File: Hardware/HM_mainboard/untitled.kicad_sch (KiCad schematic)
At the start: 13 parts, among them J1 JST PH2P ST90, Q1 PMOS - AS3401, U1 MCP73831-2, U2 TC1262-33

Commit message: Added BOM
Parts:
- C5: value 1.0UF-25V-(+80/-20%) -> 1.0uF-25V-(+80/-20%)
- C5: value 4.7u -> 4.7uF
- D2: Mouser (none) -> 10BQ015; Mouser Price/Stock (none) -> https://eu.mouser.com/ProductDetail/Vishay-Semiconductors/V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
- J1: Mouser Price/Stock (none) -> https://www.reichelt.at/at/de/jst-stiftleiste-90-1x2-polig-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; Reichelt (none) -> JST PH2P ST90
- Q1: Digikey (none) -> AS3401; Mouser Price/Stock (none) -> https://www.digikey.at/de/products/detail/anbon-semiconduct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
- R6: Mouser (none) -> RN73H1JTTD1002F100; Mouser Price/Stock (none) -> https://www.mouser.at/ProductDetail/KOA-Speer/RN73H1JTTD100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
- U1: Mouser (none) -> MCP73831T-2ACI/OT; Mouser Price/Stock (none) -> https://www.mouser.at/ProductDetail/Microchip-Technology/MC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
- U2: Mouser Price/Stock (none) -> https://www.mouser.at/ProductDetail/Microchip-Technology/TC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
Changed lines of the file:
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@@
       (effects (font (size 1.27 1.27)) (justify left))
     )
-    (property "Value" "1.0UF-25V-(+80/-20%)" (at 100.965 84.455 90)
+    (property "Value" "1.0uF-25V-(+80/-20%)" (at 100.965 84.455 90)
       (effects (font (size 1.27 1.27)) (justify left))
     )
@@
       (effects (font (size 1.27 1.27)) hide)
     )
+    (property "Reichelt" "" (at 104.775 65.405 0)
+      (effects (font (size 1.27 1.27)) hide)
+    )
     (pin "1")
     (pin "2")
@@
       (effects (font (size 1.27 1.27)) (justify left))
     )
-    (property "Value" "1.0UF-25V-(+80/-20%)" (at 144.145 78.105 90)
+    (property "Value" "1.0uF-25V-(+80/-20%)" (at 144.145 78.105 90)
       (effects (font (size 1.27 1.27)) (justify left))
     )
@@
     )
     (property "Mouser" "F921E105KPA" (at 137.795 65.405 0)
+      (effects (font (size 1.27 1.27)) hide)
+    )
+    (property "Reichelt" "" (at 137.795 65.405 0)
       (effects (font (size 1.27 1.27)) hide)
     )
@@
     )
     (property "Mouser" "ERJ-PA3J121V" (at 82.55 158.75 0)
+      (effects (font (size 1.27 1.27)) hide)
+    )
+    (property "Reichelt" "" (at 82.55 158.75 0)
       (effects (font (size 1.27 1.27)) hide)
     )
@@
       (effects (font (size 1.27 1.27)) hide)
     )
+    (property "Reichelt" "" (at 200.66 130.81 0)
+      (effects (font (size 1.27 1.27)) hide)
+    )
     (pin "1")
     (pin "2")
@@
       (effects (font (size 1.27 1.27)) hide)
     )
+    (property "Mouser Price/Stock" "https://www.reichelt.at/at/de/jst-stiftleiste-90-1x2-polig-ph-jst-ph2p-st90-p185056.html?PROVID=2807&gclid=CjwKCAiAmZGrBhAnEiwAo9qHiX8Aljedun1deSYFSHEVMIRz6JgVll-Dw5EvRr3jTF0y2CSldQKAmBoCrskQAvD_BwE" (at 52.07 146.05 0)
+      (effects (font (size 1.27 1.27)) hide)
+    )
+    (property "Reichelt" "JST PH2P ST90" (at 52.07 146.05 0)
+      (effects (font (size 1.27 1.27)) hide)
+    )
     (pin "1")
     (pin "2")
@@
       (effects (font (size 1.27 1.27)) hide)
     )
+    (property "Mouser Price/Stock" "https://www.mouser.at/ProductDetail/Microchip-Technology/TC1262-3.3VDBTR?qs=VDoAoI%2FEFTN6q7dfuakIrw%3D%3D" (at 120.015 59.055 0)
+      (effects (font (size 1.27 1.27)) hide)
+    )
+    (property "Reichelt" "" (at 120.015 59.055 0)
+      (effects (font (size 1.27 1.27)) hide)
+    )
     (pin "1")
     (pin "2")
@@
       (effects (font (size 1.27 1.27)) (justify left))
     )
-    (property "Value" "4.7u" (at 68.58 149.86 0)
+    (property "Value" "4.7uF" (at 68.58 149.86 0)
       (effects (font (size 1.27 1.27)) (justify left))
     )
@@
     )
     (property "Datasheet" "~" (at 64.77 148.59 0)
+      (effects (font (size 1.27 1.27)) hide)
+    )
+    (property "Reichelt" "" (at 64.77 148.59 0)
       (effects (font (size 1.27 1.27)) hide)
     )
@@
     )
     (property "Datasheet" "http://ww1.microchip.com/downloads/en/DeviceDoc/20001984g.pdf" (at 93.98 148.59 0)
+      (effects (font (size 1.27 1.27)) hide)
+    )
+    (property "Mouser" "MCP73831T-2ACI/OT" (at 97.79 147.32 0)
+      (effects (font (size 1.27 1.27)) hide)
+    )
+    (property "Mouser Price/Stock" "https://www.mouser.at/ProductDetail/Microchip-Technology/MCP73831T-2ACI-OT?qs=yUQqVecv4qvbBQBGbHx0Mw%3D%3D" (at 97.79 147.32 0)
+      (effects (font (size 1.27 1.27)) hide)
+    )
+    (property "Reichelt" "" (at 97.79 147.32 0)
       (effects (font (size 1.27 1.27)) hide)
     )
@@
       (effects (font (size 1.27 1.27)) hide)
     )
+    (property "Reichelt" "" (at 200.66 146.05 0)
+      (effects (font (size 1.27 1.27)) hide)
+    )
     (pin "1")
     (pin "2")
@@
       (effects (font (size 1.27 1.27)) (justify left))
     )
-    (property "Value" "4.7u" (at 143.51 146.05 0)
+    (property "Value" "4.7uF" (at 143.51 146.05 0)
       (effects (font (size 1.27 1.27)) (justify left))
     )
@@
     )
     (property "Datasheet" "~" (at 139.7 144.78 0)
+      (effects (font (size 1.27 1.27)) hide)
+    )
+    (property "Reichelt" "" (at 139.7 144.78 0)
       (effects (font (size 1.27 1.27)) hide)
     )
@@
       (effects (font (size 1.27 1.27)) hide)
     )
+    (property "Digikey" "AS3401" (at 53.975 51.435 0)
+      (effects (font (size 1.27 1.27)) hide)
+    )
+    (property "Mouser Price/Stock" "https://www.digikey.at/de/products/detail/anbon-semiconductor-int-l-limited/AS3401/16708460" (at 53.975 51.435 0)
+      (effects (font (size 1.27 1.27)) hide)
+    )
+    (property "Reichelt" "" (at 53.975 51.435 0)
+      (effects (font (size 1.27 1.27)) hide)
+    )
     (pin "1")
     (pin "2")
@@
     )
     (property "Datasheet" "" (at 41.275 59.055 0)
+      (effects (font (size 1.27 1.27)) hide)
+    )
+    (property "Reichelt" "" (at 41.275 59.055 0)
+      (effects (font (size 1.27 1.27)) hide)
+    )
+    (property "Mouser" "RN73H1JTTD1002F100" (at 41.275 59.055 0)
+      (effects (font (size 1.27 1.27)) hide)
+    )
+    (property "Mouser Price/Stock" "https://www.mouser.at/ProductDetail/KOA-Speer/RN73H1JTTD1002F100?qs=mtPtL6iy6ALCfskr2ilnpg%3D%3D" (at 41.275 59.055 0)
       (effects (font (size 1.27 1.27)) hide)
     )
@@
       (effects (font (size 1.27 1.27)) hide)
     )
-    (property "Datasheet" "" (at 51.435 59.055 0)
-      (effects (font (size 1.27 1.27)) hide)
-    )
+    (property "Datasheet" "https://eu.mouser.com/ProductDetail/Vishay-Semiconductors/VS-10BQ015-M3-5BT?qs=asPD7ZL2j3VpzaHhlDLLKA%3D%3D&gad_source=1&gclid=CjwKCAiA1MCrBhAoEiwAC2d64Qfz9GdFJXcJop1dluLSezxhXfgrxGSJlfwXR4mOBbP2oq8S6QpdJRoCLncQAvD_BwE" (at 51.435 59.055 0)
+      (effects (font (size 1.27 1.27)) hide)
+    )
+    (property "Mouser" "10BQ015" (at 51.435 59.055 0)
+      (effects (font (size 1.27 1.27)) hide)
+    )
+    (property "Mouser Price/Stock" "https://eu.mouser.com/ProductDetail/Vishay-Semiconductors/VS-10BQ015-M3-5BT?qs=asPD7ZL2j3VpzaHhlDLLKA%3D%3D&gad_source=1&gclid=CjwKCAiA1MCrBhAoEiwAC2d64Qfz9GdFJXcJop1dluLSezxhXfgrxGSJlfwXR4mOBbP2oq8S6QpdJRoCLncQAvD_BwE" (at 51.435 59.055 0)
+      (effects (font (size 1.27 1.27)) hide)
+    )
+    (property "Reichelt" "" (at 51.435 59.055 0)
+      (effects (font (size 1.27 1.27)) hide)
+    )

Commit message: Updated BOM
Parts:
- C5: Mouser F921E105KPA -> 647-F921E105KPA
- C5: Mouser (none) -> 81-GRM188Z71A475KE5J
- D2: Mouser 10BQ015 -> 78-VS-10BQ015-M35BT
- Q1: value PMOS - AS3401 -> PMV27UPEAR; Digikey AS3401 -> 4530-AS3401CT; Mouser (none) -> 771-PMV27UPEAR
- R6: Mouser ERJ-PA3J121V -> 71-CRCW06032K00FKEAC
- R6: value 10k -> 10k/1%; Mouser ERJ-PA3J121V -> 660-RN73H1JT1002F100
- R6: Mouser RN73H1JTTD1002F100 -> 660-RN73H1JT1002F100
- U1: Mouser MCP73831T-2ACI/OT -> 579-MCP73831T-2ACIOT
- U2: Mouser TC1262-3.3VDBTR -> 579-TC1262-3.3VDBTR
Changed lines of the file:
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@@
       (effects (font (size 1.27 1.27)) hide)
     )
-    (property "Mouser" "F921E105KPA" (at 104.775 65.405 0)
+    (property "Mouser" "647-F921E105KPA" (at 104.775 65.405 0)
       (effects (font (size 1.27 1.27)) hide)
     )
@@
       (effects (font (size 1.27 1.27)) hide)
     )
-    (property "Mouser" "F921E105KPA" (at 137.795 65.405 0)
+    (property "Mouser" "647-F921E105KPA" (at 137.795 65.405 0)
       (effects (font (size 1.27 1.27)) hide)
     )
@@
       (effects (font (size 1.27 1.27)) hide)
     )
-    (property "Mouser" "ERJ-PA3J121V" (at 82.55 158.75 0)
+    (property "Mouser" "71-CRCW06032K00FKEAC" (at 82.55 158.75 0)
       (effects (font (size 1.27 1.27)) hide)
     )
@@
       (effects (font (size 1.778 1.778)) (justify left bottom))
     )
-    (property "Value" "10k" (at 199.39 129.54 0)
+    (property "Value" "10k/1%" (at 199.39 129.54 0)
       (effects (font (size 1.778 1.778)) (justify left bottom))
     )
@@
       (effects (font (size 1.27 1.27)) hide)
     )
-    (property "Mouser" "ERJ-PA3J121V" (at 200.66 130.81 0)
+    (property "Mouser" "660-RN73H1JT1002F100" (at 200.66 130.81 0)
       (effects (font (size 1.27 1.27)) hide)
     )
@@
       (effects (font (size 1.27 1.27)) hide)
     )
-    (property "Mouser" "TC1262-3.3VDBTR" (at 120.015 59.055 0)
+    (property "Mouser" "579-TC1262-3.3VDBTR" (at 120.015 59.055 0)
       (effects (font (size 1.27 1.27)) hide)
     )
@@
       (effects (font (size 1.27 1.27)) hide)
     )
+    (property "Mouser" "81-GRM188Z71A475KE5J" (at 64.77 148.59 0)
+      (effects (font (size 1.27 1.27)) hide)
+    )
     (pin "1")
     (pin "2")
@@
       (effects (font (size 1.27 1.27)) hide)
     )
-    (property "Mouser" "MCP73831T-2ACI/OT" (at 97.79 147.32 0)
+    (property "Mouser" "579-MCP73831T-2ACIOT" (at 97.79 147.32 0)
       (effects (font (size 1.27 1.27)) hide)
     )
@@
       (effects (font (size 1.778 1.778)) (justify left bottom))
     )
-    (property "Value" "10k" (at 199.39 144.78 0)
+    (property "Value" "10k/1%" (at 199.39 144.78 0)
       (effects (font (size 1.778 1.778)) (justify left bottom))
     )
@@
       (effects (font (size 1.27 1.27)) hide)
     )
-    (property "Mouser" "ERJ-PA3J121V" (at 200.66 146.05 0)
+    (property "Mouser" "660-RN73H1JT1002F100" (at 200.66 146.05 0)
       (effects (font (size 1.27 1.27)) hide)
     )
@@
       (effects (font (size 1.27 1.27)) hide)
     )
+    (property "Mouser" "81-GRM188Z71A475KE5J" (at 139.7 144.78 0)
+      (effects (font (size 1.27 1.27)) hide)
+    )
     (pin "1")
     (pin "2")
@@
       (effects (font (size 1.27 1.27)) (justify left))
     )
-    (property "Value" "PMOS - AS3401" (at 59.055 50.165 0)
+    (property "Value" "PMV27UPEAR" (at 59.055 50.165 0)
       (effects (font (size 1.27 1.27)) (justify left))
     )
@@
       (effects (font (size 1.27 1.27)) hide)
     )
-    (property "Digikey" "AS3401" (at 53.975 51.435 0)
+    (property "Digikey" "4530-AS3401CT" (at 53.975 51.435 0)
       (effects (font (size 1.27 1.27)) hide)
     )
@@
     )
     (property "Reichelt" "" (at 53.975 51.435 0)
+      (effects (font (size 1.27 1.27)) hide)
+    )
+    (property "Mouser" "771-PMV27UPEAR" (at 53.975 51.435 0)
       (effects (font (size 1.27 1.27)) hide)
     )
@@
       (effects (font (size 1.27 1.27)) hide)
     )
-    (property "Mouser" "RN73H1JTTD1002F100" (at 41.275 59.055 0)
+    (property "Mouser" "660-RN73H1JT1002F100" (at 41.275 59.055 0)
       (effects (font (size 1.27 1.27)) hide)
     )
@@
       (effects (font (size 1.27 1.27)) hide)
     )
-    (property "Mouser" "10BQ015" (at 51.435 59.055 0)
-      (effects (font (size 1.27 1.27)) hide)
-    )
+    (property "Mouser" "78-VS-10BQ015-M35BT" (at 51.435 59.055 0)
+      (effects (font (size 1.27 1.27)) hide)
+    )

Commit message: Updated BOM
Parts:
- C5: Mouser 647-F921E105KPA -> F921E105KPA
- C5: Mouser 81-GRM188Z71A475KE5J -> (none)
- D2: Mouser 78-VS-10BQ015-M35BT -> 10BQ015
- Q1: value PMV27UPEAR -> PMOS - AS3401; Digikey 4530-AS3401CT -> AS3401; Mouser 771-PMV27UPEAR -> (none)
- R6: Mouser 71-CRCW06032K00FKEAC -> ERJ-PA3J121V
- R6: value 10k/1% -> 10k; Mouser 660-RN73H1JT1002F100 -> ERJ-PA3J121V
- R6: Mouser 660-RN73H1JT1002F100 -> RN73H1JTTD1002F100
- U1: Mouser 579-MCP73831T-2ACIOT -> MCP73831T-2ACI/OT
- U2: Mouser 579-TC1262-3.3VDBTR -> TC1262-3.3VDBTR
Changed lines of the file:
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@@
       (effects (font (size 1.27 1.27)) hide)
     )
-    (property "Mouser" "647-F921E105KPA" (at 104.775 65.405 0)
+    (property "Mouser" "F921E105KPA" (at 104.775 65.405 0)
       (effects (font (size 1.27 1.27)) hide)
     )
@@
       (effects (font (size 1.27 1.27)) hide)
     )
-    (property "Mouser" "647-F921E105KPA" (at 137.795 65.405 0)
+    (property "Mouser" "F921E105KPA" (at 137.795 65.405 0)
       (effects (font (size 1.27 1.27)) hide)
     )
@@
       (effects (font (size 1.27 1.27)) hide)
     )
-    (property "Mouser" "71-CRCW06032K00FKEAC" (at 82.55 158.75 0)
+    (property "Mouser" "ERJ-PA3J121V" (at 82.55 158.75 0)
       (effects (font (size 1.27 1.27)) hide)
     )
@@
       (effects (font (size 1.778 1.778)) (justify left bottom))
     )
-    (property "Value" "10k/1%" (at 199.39 129.54 0)
+    (property "Value" "10k" (at 199.39 129.54 0)
       (effects (font (size 1.778 1.778)) (justify left bottom))
     )
@@
       (effects (font (size 1.27 1.27)) hide)
     )
-    (property "Mouser" "660-RN73H1JT1002F100" (at 200.66 130.81 0)
+    (property "Mouser" "ERJ-PA3J121V" (at 200.66 130.81 0)
       (effects (font (size 1.27 1.27)) hide)
     )
@@
       (effects (font (size 1.27 1.27)) hide)
     )
-    (property "Mouser" "579-TC1262-3.3VDBTR" (at 120.015 59.055 0)
+    (property "Mouser" "TC1262-3.3VDBTR" (at 120.015 59.055 0)
       (effects (font (size 1.27 1.27)) hide)
     )
@@
       (effects (font (size 1.27 1.27)) hide)
     )
-    (property "Mouser" "81-GRM188Z71A475KE5J" (at 64.77 148.59 0)
-      (effects (font (size 1.27 1.27)) hide)
-    )
     (pin "1")
     (pin "2")
@@
       (effects (font (size 1.27 1.27)) hide)
     )
-    (property "Mouser" "579-MCP73831T-2ACIOT" (at 97.79 147.32 0)
+    (property "Mouser" "MCP73831T-2ACI/OT" (at 97.79 147.32 0)
       (effects (font (size 1.27 1.27)) hide)
     )
@@
       (effects (font (size 1.778 1.778)) (justify left bottom))
     )
-    (property "Value" "10k/1%" (at 199.39 144.78 0)
+    (property "Value" "10k" (at 199.39 144.78 0)
       (effects (font (size 1.778 1.778)) (justify left bottom))
     )
@@
       (effects (font (size 1.27 1.27)) hide)
     )
-    (property "Mouser" "660-RN73H1JT1002F100" (at 200.66 146.05 0)
+    (property "Mouser" "ERJ-PA3J121V" (at 200.66 146.05 0)
       (effects (font (size 1.27 1.27)) hide)
     )
@@
       (effects (font (size 1.27 1.27)) hide)
     )
-    (property "Mouser" "81-GRM188Z71A475KE5J" (at 139.7 144.78 0)
-      (effects (font (size 1.27 1.27)) hide)
-    )
     (pin "1")
     (pin "2")
@@
       (effects (font (size 1.27 1.27)) (justify left))
     )
-    (property "Value" "PMV27UPEAR" (at 59.055 50.165 0)
+    (property "Value" "PMOS - AS3401" (at 59.055 50.165 0)
       (effects (font (size 1.27 1.27)) (justify left))
     )
@@
       (effects (font (size 1.27 1.27)) hide)
     )
-    (property "Digikey" "4530-AS3401CT" (at 53.975 51.435 0)
+    (property "Digikey" "AS3401" (at 53.975 51.435 0)
       (effects (font (size 1.27 1.27)) hide)
     )
@@
     )
     (property "Reichelt" "" (at 53.975 51.435 0)
-      (effects (font (size 1.27 1.27)) hide)
-    )
-    (property "Mouser" "771-PMV27UPEAR" (at 53.975 51.435 0)
       (effects (font (size 1.27 1.27)) hide)
     )
@@
       (effects (font (size 1.27 1.27)) hide)
     )
-    (property "Mouser" "660-RN73H1JT1002F100" (at 41.275 59.055 0)
+    (property "Mouser" "RN73H1JTTD1002F100" (at 41.275 59.055 0)
       (effects (font (size 1.27 1.27)) hide)
     )
@@
       (effects (font (size 1.27 1.27)) hide)
     )
-    (property "Mouser" "78-VS-10BQ015-M35BT" (at 51.435 59.055 0)
-      (effects (font (size 1.27 1.27)) hide)
-    )
+    (property "Mouser" "10BQ015" (at 51.435 59.055 0)
+      (effects (font (size 1.27 1.27)) hide)
+    )

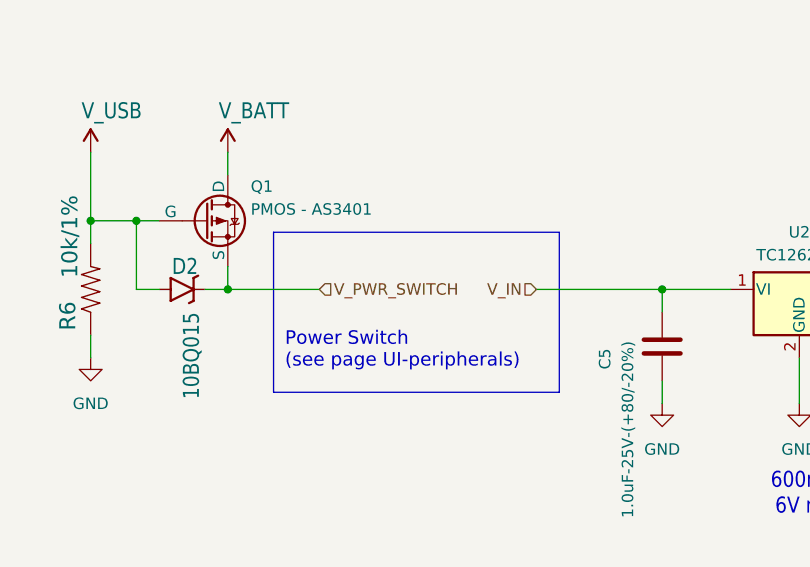
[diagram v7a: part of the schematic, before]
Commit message: Fixed wrong symbol-to-footprint assignment of PMOS AS3401
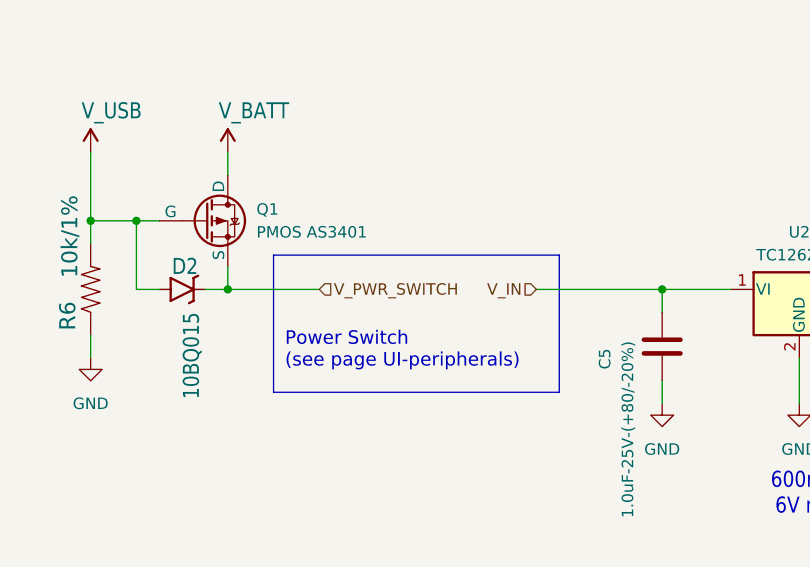
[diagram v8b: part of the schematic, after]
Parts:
- removed Q1: PMOS - AS3401, Package_TO_SOT_SMD:SOT-23, symbol Simulation_SPICE:PMOS
- added Q1: PMOS AS3401, Package_TO_SOT_SMD:TSOT-23_HandSoldering, symbol HeadMouse:AS3401
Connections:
- net V_BATT: now also Q1.3 (D)
- net V_PWR_SWITCH: now also Q1.2 (S)
- net V_USB: now also Q1.1 (G)
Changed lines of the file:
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@@
     (fill (type none))
   )
-  (rectangle (start 61.595 52.705) (end 93.345 70.485)
+  (rectangle (start 61.595 55.245) (end 93.345 70.485)
     (stroke (width 0) (type default))
     (fill (type none))
@@
     )
   )
+  (symbol (lib_id "HeadMouse:AS3401") (at 53.975 51.435 0) (unit 1)
+    (in_bom yes) (on_board yes) (dnp no) (fields_autoplaced)
+    (property "Reference" "Q1" (at 59.69 50.165 0)
+      (effects (font (size 1.27 1.27)) (justify left))
+    )
+    (property "Value" "PMOS AS3401" (at 59.69 52.705 0)
+      (effects (font (size 1.27 1.27)) (justify left))
+    )
+    (property "Footprint" "Package_TO_SOT_SMD:TSOT-23_HandSoldering" (at 59.055 48.895 0)
+      (effects (font (size 1.27 1.27)) hide)
+    )
+    (property "Datasheet" "https://ngspice.sourceforge.io/docs/ngspice-manual.pdf" (at 53.975 64.135 0)
+      (effects (font (size 1.27 1.27)) hide)
+    )
+    (property "Sim.Device" "PMOS" (at 53.975 68.58 0)
+      (effects (font (size 1.27 1.27)) hide)
+    )
+    (property "Sim.Type" "VDMOS" (at 53.975 70.485 0)
+      (effects (font (size 1.27 1.27)) hide)
+    )
+    (property "Sim.Pins" "1=D 2=G 3=S" (at 53.975 66.675 0)
+      (effects (font (size 1.27 1.27)) hide)
+    )
+    (pin "1")
+    (pin "2")
+    (pin "3")
+    (instances
+      (project "HM_mainboard"
+        (path "/54a6df43-5475-46a2-9916-8b0260700d4c/b19d5209-4861-4a96-a3d1-daca4a23de52"
+          (reference "Q1") (unit 1)
+        )
+      )
+    )
+  )
   (symbol (lib_name "GND_1") (lib_id "power:GND") (at 97.79 156.21 0) (unit 1)
     (in_bom yes) (on_board yes) (dnp no) (fields_autoplaced)
@@
         )
       )
-    )
-  )
-  (symbol (lib_id "Simulation_SPICE:PMOS") (at 53.975 51.435 0) (unit 1)
-    (in_bom yes) (on_board yes) (dnp no)
-    (property "Reference" "Q1" (at 59.055 47.625 0)
-      (effects (font (size 1.27 1.27)) (justify left))
-    )
-    (property "Value" "PMOS - AS3401" (at 59.055 50.165 0)
-      (effects (font (size 1.27 1.27)) (justify left))
-    )
-    (property "Footprint" "Package_TO_SOT_SMD:SOT-23" (at 59.055 48.895 0)
-      (effects (font (size 1.27 1.27)) hide)
-    )
-    (property "Datasheet" "https://mm.digikey.com/Volume0/opasdata/d220001/medias/docus/2779/AS3401.pdf" (at 53.975 64.135 0)
-      (effects (font (size 1.27 1.27)) hide)
-    )
-    (property "Sim.Device" "PMOS" (at 53.975 68.58 0)
-      (effects (font (size 1.27 1.27)) hide)
-    )
-    (property "Sim.Type" "VDMOS" (at 53.975 70.485 0)
-      (effects (font (size 1.27 1.27)) hide)
-    )
-    (property "Sim.Pins" "1=D 2=G 3=S" (at 53.975 66.675 0)
-      (effects (font (size 1.27 1.27)) hide)
-    )
-    (property "Digikey" "AS3401" (at 53.975 51.435 0)
-      (effects (font (size 1.27 1.27)) hide)
-    )
-    (property "Mouser Price/Stock" "https://www.digikey.at/de/products/detail/anbon-semiconductor-int-l-limited/AS3401/16708460" (at 53.975 51.435 0)
-      (effects (font (size 1.27 1.27)) hide)
-    )
-    (property "Reichelt" "" (at 53.975 51.435 0)
-      (effects (font (size 1.27 1.27)) hide)
-    )
-    (pin "1")
-    (pin "2")
-    (pin "3")
-    (instances
-      (project "HM_mainboard"
-        (path "/54a6df43-5475-46a2-9916-8b0260700d4c/b19d5209-4861-4a96-a3d1-daca4a23de52"
-          (reference "Q1") (unit 1)
-        )
-      )
